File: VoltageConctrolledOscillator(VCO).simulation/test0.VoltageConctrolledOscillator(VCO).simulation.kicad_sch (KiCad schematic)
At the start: 18 parts, among them Q1 NPN

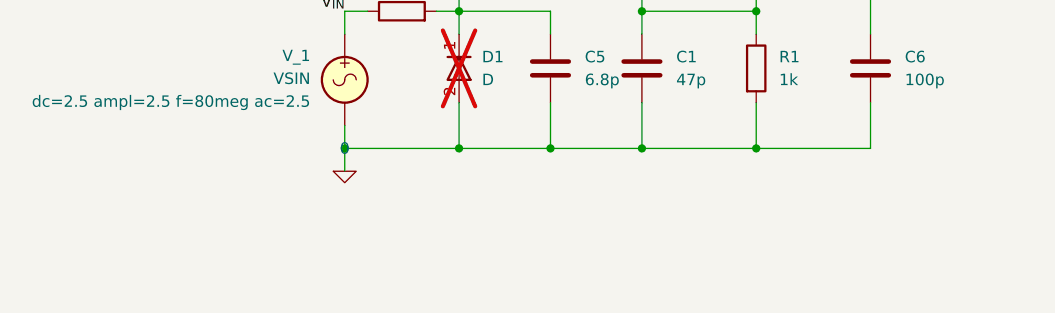
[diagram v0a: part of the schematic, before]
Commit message: Implement second version of VCO
* Implement subseets for VCO tests.
* Test 0 is excluded from simulations.
* Test 1 schematic taken from The Art of Electronic (third edition
  improved) Figure 4.83 p. 267. This one gives pretty good results.
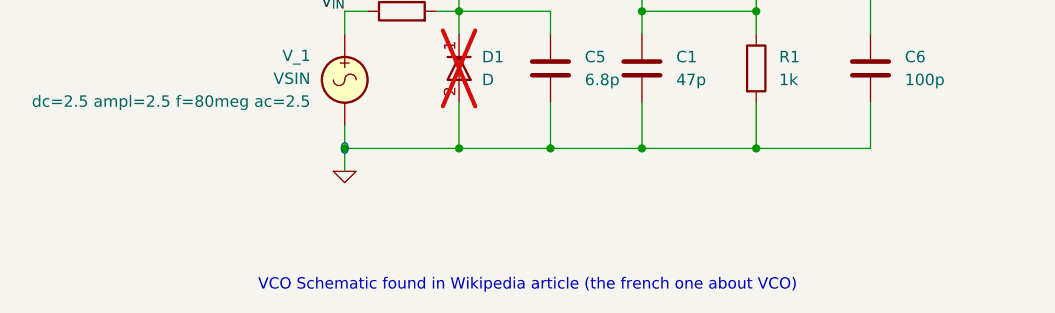
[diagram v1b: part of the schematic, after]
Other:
- note added: "VCO Schematic found in Wikipedia article (the french one about VCO)"
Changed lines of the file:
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@@
+		)
+	)
+	(text "VCO Schematic found in Wikipedia article (the french one about VCO)"
+		(exclude_from_sim no)
+		(at 127 147.32 0)
+		(effects
+			(font
+				(size 1.25 1.25)
+			)
+			(href "https://fr.wikipedia.org/wiki/Oscillateur_command%C3%A9_en_tension#/media/Fichier:VCO_80_MHz.png")
 		)
 	)
@@
 		(at 113.03 116.84 90)
 		(unit 1)
-		(exclude_from_sim no)
+		(exclude_from_sim yes)
 		(in_bom yes)
 		(on_board yes)
@@
 		(instances
 			(project "VoltageConctrolledOscillator(VCO).simulation"
-				(path "/1ef713ee-5208-45bb-a886-68d3bad2ed43"
+				(path "/39e238e2-77a8-4917-9f90-31fbe07c1d9b/a3a5a66e-2836-4c13-8331-37a2c9b1332c"
 					(reference "R4")
 					(unit 1)
@@
 		(at 171.45 96.52 90)
 		(unit 1)
-		(exclude_from_sim no)
+		(exclude_from_sim yes)
 		(in_bom yes)
 		(on_board yes)
@@
 		(instances
 			(project "VoltageConctrolledOscillator(VCO).simulation"
-				(path "/1ef713ee-5208-45bb-a886-68d3bad2ed43"
+				(path "/39e238e2-77a8-4917-9f90-31fbe07c1d9b/a3a5a66e-2836-4c13-8331-37a2c9b1332c"
 					(reference "C7")
 					(unit 1)
@@
 		(at 146.05 81.28 270)
 		(unit 1)
-		(exclude_from_sim no)
+		(exclude_from_sim yes)
 		(in_bom yes)
 		(on_board yes)
@@
 		(instances
 			(project "VoltageConctrolledOscillator(VCO).simulation"
-				(path "/1ef713ee-5208-45bb-a886-68d3bad2ed43"
+				(path "/39e238e2-77a8-4917-9f90-31fbe07c1d9b/a3a5a66e-2836-4c13-8331-37a2c9b1332c"
 					(reference "C4")
 					(unit 1)
@@
 		(at 106.68 134.62 0)
 		(unit 1)
-		(exclude_from_sim no)
+		(exclude_from_sim yes)
 		(in_bom yes)
 		(on_board yes)
@@
 		(instances
 			(project "VoltageConctrolledOscillator(VCO).simulation"
-				(path "/1ef713ee-5208-45bb-a886-68d3bad2ed43"
+				(path "/39e238e2-77a8-4917-9f90-31fbe07c1d9b/a3a5a66e-2836-4c13-8331-37a2c9b1332c"
 					(reference "#GND02")
 					(unit 1)
@@
 		(at 139.7 110.49 0)
 		(unit 1)
-		(exclude_from_sim no)
+		(exclude_from_sim yes)
 		(in_bom yes)
 		(on_board yes)
@@
 		(instances
 			(project "VoltageConctrolledOscillator(VCO).simulation"
-				(path "/1ef713ee-5208-45bb-a886-68d3bad2ed43"
+				(path "/39e238e2-77a8-4917-9f90-31fbe07c1d9b/a3a5a66e-2836-4c13-8331-37a2c9b1332c"
 					(reference "C2")
 					(unit 1)
@@
 		(at 139.7 123.19 0)
 		(unit 1)
-		(exclude_from_sim no)
+		(exclude_from_sim yes)
 		(in_bom yes)
 		(on_board yes)
@@
 				)
 			)
+			(project ""
+				(path "/39e238e2-77a8-4917-9f90-31fbe07c1d9b/a3a5a66e-2836-4c13-8331-37a2c9b1332c"
+					(reference "C1")
+					(unit 1)
+				)
+			)
 		)
 	)
@@
 		(at 146.05 93.98 90)
 		(unit 1)
-		(exclude_from_sim no)
+		(exclude_from_sim yes)
 		(in_bom yes)
 		(on_board yes)
@@
 		(instances
 			(project "VoltageConctrolledOscillator(VCO).simulation"
-				(path "/1ef713ee-5208-45bb-a886-68d3bad2ed43"
+				(path "/39e238e2-77a8-4917-9f90-31fbe07c1d9b/a3a5a66e-2836-4c13-8331-37a2c9b1332c"
 					(reference "R3")
 					(unit 1)
@@
 		(at 152.4 68.58 0)
 		(unit 1)
-		(exclude_from_sim no)
+		(exclude_from_sim yes)
 		(in_bom yes)
 		(on_board yes)
@@
 		(instances
 			(project "VoltageConctrolledOscillator(VCO).simulation"
-				(path "/1ef713ee-5208-45bb-a886-68d3bad2ed43"
+				(path "/39e238e2-77a8-4917-9f90-31fbe07c1d9b/a3a5a66e-2836-4c13-8331-37a2c9b1332c"
 					(reference "#PWR01")
 					(unit 1)
@@
 		(mirror y)
 		(unit 1)
-		(exclude_from_sim no)
+		(exclude_from_sim yes)
 		(in_bom yes)
 		(on_board yes)
@@
 				)
 			)
+			(project ""
+				(path "/39e238e2-77a8-4917-9f90-31fbe07c1d9b/a3a5a66e-2836-4c13-8331-37a2c9b1332c"
+					(reference "V_1")
+					(unit 1)
+				)
+			)
 		)
 	)
@@
 				)
 			)
+			(project ""
+				(path "/39e238e2-77a8-4917-9f90-31fbe07c1d9b/a3a5a66e-2836-4c13-8331-37a2c9b1332c"
+					(reference "D1")
+					(unit 1)
+				)
+			)
 		)
 	)
@@
 		(at 152.4 74.93 180)
 		(unit 1)
-		(exclude_from_sim no)
+		(exclude_from_sim yes)
 		(in_bom yes)
 		(on_board yes)
@@
 		(instances
 			(project "VoltageConctrolledOscillator(VCO).simulation"
-				(path "/1ef713ee-5208-45bb-a886-68d3bad2ed43"
+				(path "/39e238e2-77a8-4917-9f90-31fbe07c1d9b/a3a5a66e-2836-4c13-8331-37a2c9b1332c"
 					(reference "R6")
 					(unit 1)
@@
 		(at 133.35 104.14 270)
 		(unit 1)
-		(exclude_from_sim no)
+		(exclude_from_sim yes)
 		(in_bom yes)
 		(on_board yes)
@@
 		(instances
 			(project "VoltageConctrolledOscillator(VCO).simulation"
-				(path "/1ef713ee-5208-45bb-a886-68d3bad2ed43"
+				(path "/39e238e2-77a8-4917-9f90-31fbe07c1d9b/a3a5a66e-2836-4c13-8331-37a2c9b1332c"
 					(reference "C3")
 					(unit 1)
@@
 		(at 149.86 104.14 0)
 		(unit 1)
-		(exclude_from_sim no)
+		(exclude_from_sim yes)
 		(in_bom yes)
 		(on_board yes)
@@
 				)
 			)
+			(project ""
+				(path "/39e238e2-77a8-4917-9f90-31fbe07c1d9b/a3a5a66e-2836-4c13-8331-37a2c9b1332c"
+					(reference "Q1")
+					(unit 1)
+				)
+			)
 		)
 	)
@@
 		(at 119.38 110.49 180)
 		(unit 1)
-		(exclude_from_sim no)
+		(exclude_from_sim yes)
 		(in_bom yes)
 		(on_board yes)
@@
 				)
 			)
+			(project ""
+				(path "/39e238e2-77a8-4917-9f90-31fbe07c1d9b/a3a5a66e-2836-4c13-8331-37a2c9b1332c"
+					(reference "L1")
+					(unit 1)
+				)
+			)
 		)
 	)
@@
 		(at 60.706 116.84 0)
 		(unit 1)
-		(exclude_from_sim no)
+		(exclude_from_sim yes)
 		(in_bom yes)
 		(on_board yes)
@@
 				)
 			)
+			(project ""
+				(path "/39e238e2-77a8-4917-9f90-31fbe07c1d9b/a3a5a66e-2836-4c13-8331-37a2c9b1332c"
+					(reference "#PWR02")
+					(unit 1)
+				)
+			)
 		)
 	)
@@
 		(at 127 93.98 270)
 		(unit 1)
-		(exclude_from_sim no)
+		(exclude_from_sim yes)
 		(in_bom yes)
 		(on_board yes)
@@
 		(instances
 			(project "VoltageConctrolledOscillator(VCO).simulation"
-				(path "/1ef713ee-5208-45bb-a886-68d3bad2ed43"
+				(path "/39e238e2-77a8-4917-9f90-31fbe07c1d9b/a3a5a66e-2836-4c13-8331-37a2c9b1332c"
 					(reference "#GND07")
 					(unit 1)
@@
 		(at 133.35 93.98 90)
 		(unit 1)
-		(exclude_from_sim no)
+		(exclude_from_sim yes)
 		(in_bom yes)
 		(on_board yes)
@@
 		(instances
 			(project "VoltageConctrolledOscillator(VCO).simulation"
-				(path "/1ef713ee-5208-45bb-a886-68d3bad2ed43"
+				(path "/39e238e2-77a8-4917-9f90-31fbe07c1d9b/a3a5a66e-2836-4c13-8331-37a2c9b1332c"
 					(reference "R2")
 					(unit 1)
@@
 		(at 60.706 124.46 0)
 		(unit 1)
-		(exclude_from_sim no)
+		(exclude_from_sim yes)
 		(in_bom yes)
 		(on_board yes)
@@
 				)
 			)
+			(project ""
+				(path "/39e238e2-77a8-4917-9f90-31fbe07c1d9b/a3a5a66e-2836-4c13-8331-37a2c9b1332c"
+					(reference "V_0")
+					(unit 1)
+				)
+			)
 		)
 	)
@@
 		(at 60.706 132.08 0)
 		(unit 1)
-		(exclude_from_sim no)
+		(exclude_from_sim yes)
 		(in_bom yes)
 		(on_board yes)
@@
 		(instances
 			(project "VoltageConctrolledOscillator(VCO).simulation"
-				(path "/1ef713ee-5208-45bb-a886-68d3bad2ed43"
+				(path "/39e238e2-77a8-4917-9f90-31fbe07c1d9b/a3a5a66e-2836-4c13-8331-37a2c9b1332c"
 					(reference "#GND01")
 					(unit 1)
@@
 		(at 139.7 81.28 270)
 		(unit 1)
-		(exclude_from_sim no)
+		(exclude_from_sim yes)
 		(in_bom yes)
 		(on_board yes)
@@
 		(instances
 			(project "VoltageConctrolledOscillator(VCO).simulation"
-				(path "/1ef713ee-5208-45bb-a886-68d3bad2ed43"
+				(path "/39e238e2-77a8-4917-9f90-31fbe07c1d9b/a3a5a66e-2836-4c13-8331-37a2c9b1332c"
 					(reference "#GND06")
 					(unit 1)
@@
 		(at 129.54 123.19 0)
 		(unit 1)
-		(exclude_from_sim no)
+		(exclude_from_sim yes)
 		(in_bom yes)
 		(on_board yes)
@@
 		(instances
 			(project "VoltageConctrolledOscillator(VCO).simulation"
-				(path "/1ef713ee-5208-45bb-a886-68d3bad2ed43"
+				(path "/39e238e2-77a8-4917-9f90-31fbe07c1d9b/a3a5a66e-2836-4c13-8331-37a2c9b1332c"
 					(reference "C5")
 					(unit 1)
@@
 		(at 152.4 123.19 0)
 		(unit 1)
-		(exclude_from_sim no)
+		(exclude_from_sim yes)
 		(in_bom yes)
 		(on_board yes)
@@
 				)
 			)
+			(project ""
+				(path "/39e238e2-77a8-4917-9f90-31fbe07c1d9b/a3a5a66e-2836-4c13-8331-37a2c9b1332c"
+					(reference "R1")
+					(unit 1)
+				)
+			)
 		)
 	)
@@
 		(at 165.1 123.19 0)
 		(unit 1)
-		(exclude_from_sim no)
+		(exclude_from_sim yes)
 		(in_bom yes)
 		(on_board yes)
@@
 		(instances
 			(project "VoltageConctrolledOscillator(VCO).simulation"
-				(path "/1ef713ee-5208-45bb-a886-68d3bad2ed43"
+				(path "/39e238e2-77a8-4917-9f90-31fbe07c1d9b/a3a5a66e-2836-4c13-8331-37a2c9b1332c"
 					(reference "C6")
 					(unit 1)
@@
 		(at 152.4 87.63 180)
 		(unit 1)
-		(exclude_from_sim no)
+		(exclude_from_sim yes)
 		(in_bom yes)
 		(on_board yes)
@@
 		(instances
 			(project "VoltageConctrolledOscillator(VCO).simulation"
-				(path "/1ef713ee-5208-45bb-a886-68d3bad2ed43"
+				(path "/39e238e2-77a8-4917-9f90-31fbe07c1d9b/a3a5a66e-2836-4c13-8331-37a2c9b1332c"
 					(reference "R5")
 					(unit 1)
@@
 		)
 	)
-	(sheet_instances
-		(path "/"
-			(page "1")
-		)
-	)

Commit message: Rearrange sheets
Move stuff around sheets for future project evolution :
* Voltage sources are moved on top hierarchical page
* Hierarchical label is used to set input voltage to Test 1 sheet
* Add text on Test 0 sheet
* All subsheet page are A5 size for ease of read reason.
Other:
- note added: "(This is the french article about VCO)"
- note added: "Excluded from simulation"
- note added: "VCO Schematic found in Wikipedia article"
- note removed: "VCO Schematic found in Wikipedia article (the french one about VCO)"
- moved on the sheet: C1, C2, C3, C4, C5, C6, C7, D1, L1, Q1, R1, R2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
